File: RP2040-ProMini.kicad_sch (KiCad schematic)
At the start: 42 parts, among them J1 CONN_L, J2 CONN_U, J3 CONN_R2, J4 CONN_R, J5 CONN_R3, Q1 AO3400A, U1 W25Q128JVS, U2 RP2040, U3 TPS63060, U4 W25Q128JVEIQ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

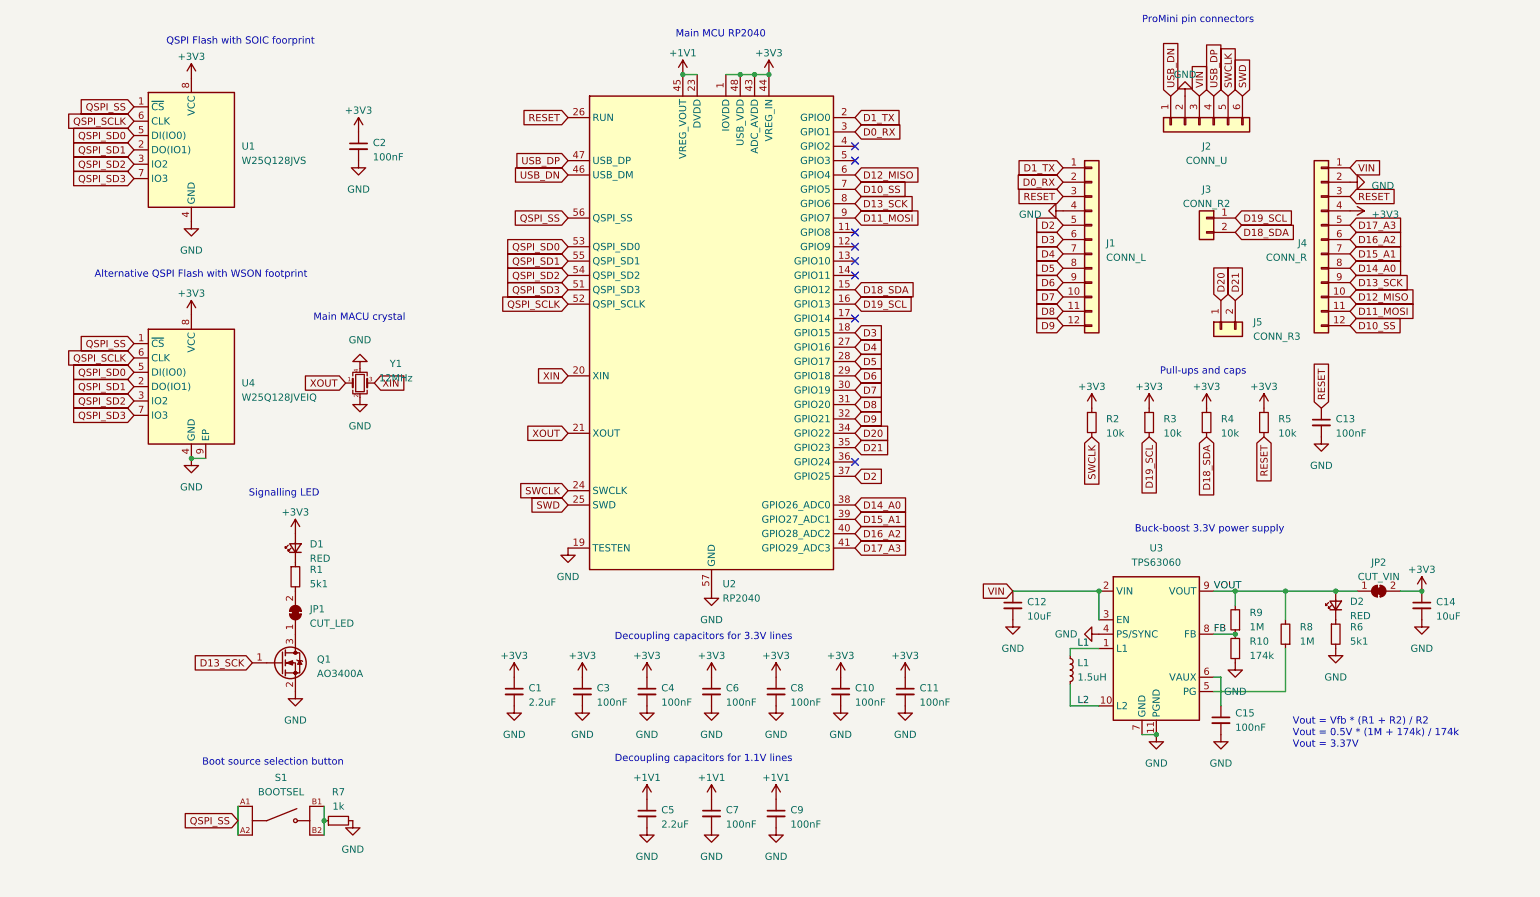
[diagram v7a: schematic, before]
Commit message: Aligned schematics components to bigger grid
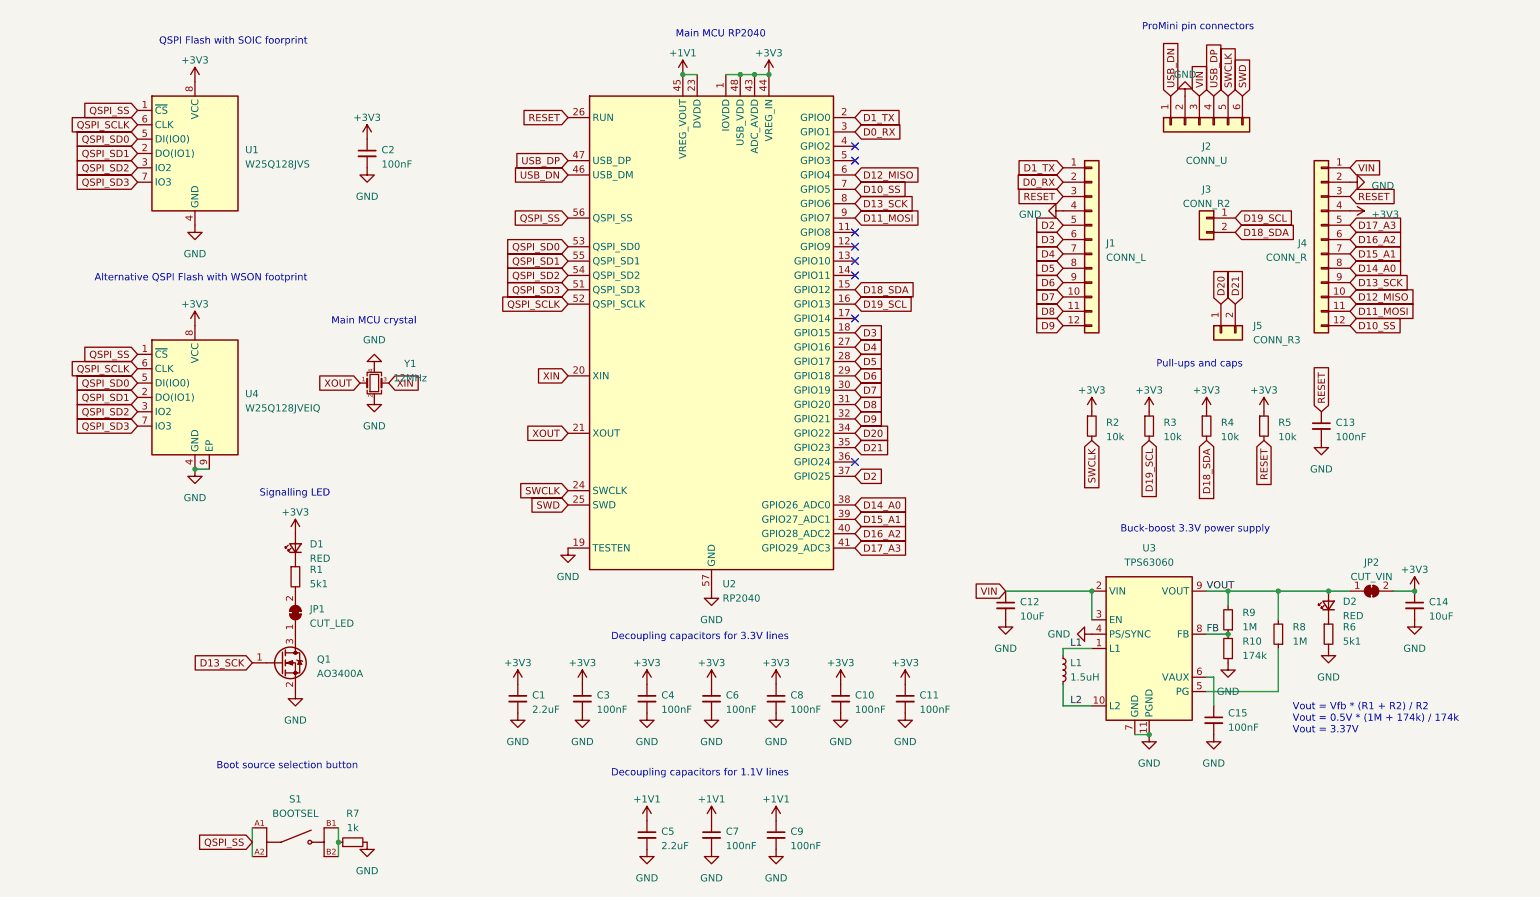
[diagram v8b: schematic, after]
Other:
- note added: "Main MCU crystal"
- note removed: "Main MACU crystal"
- moved on the sheet: C1, C10, C11, C12, C13, C14, C15, C2, C3, C4, C5, C6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
